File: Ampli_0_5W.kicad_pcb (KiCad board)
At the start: 2 copper layers, 100 x 100 mm, 71 parts, among them J1 RF_In, J2 PTT_In, J3 Aux_PTT_Out, J4 RF_Out, J5 RF_Out, J6 RF_Out, Q1 2N7002, Q2 FDD6685, Q3 2N5109, Q4 AFT05MP075N, T1 4:1, T2 1:1, T3 1:9, U1 LM78M05_TO252

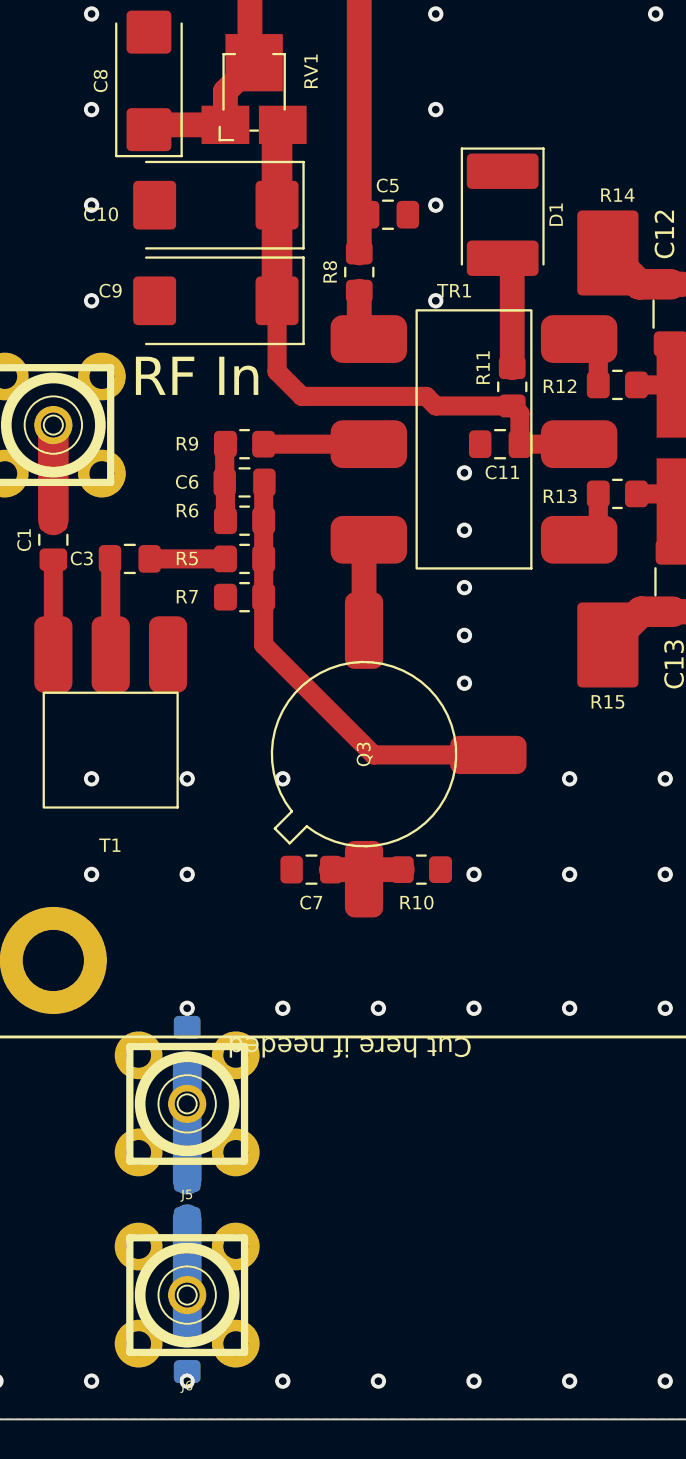
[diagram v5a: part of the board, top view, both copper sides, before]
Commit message: Kicad 7, new iBom, new temp diode cabling
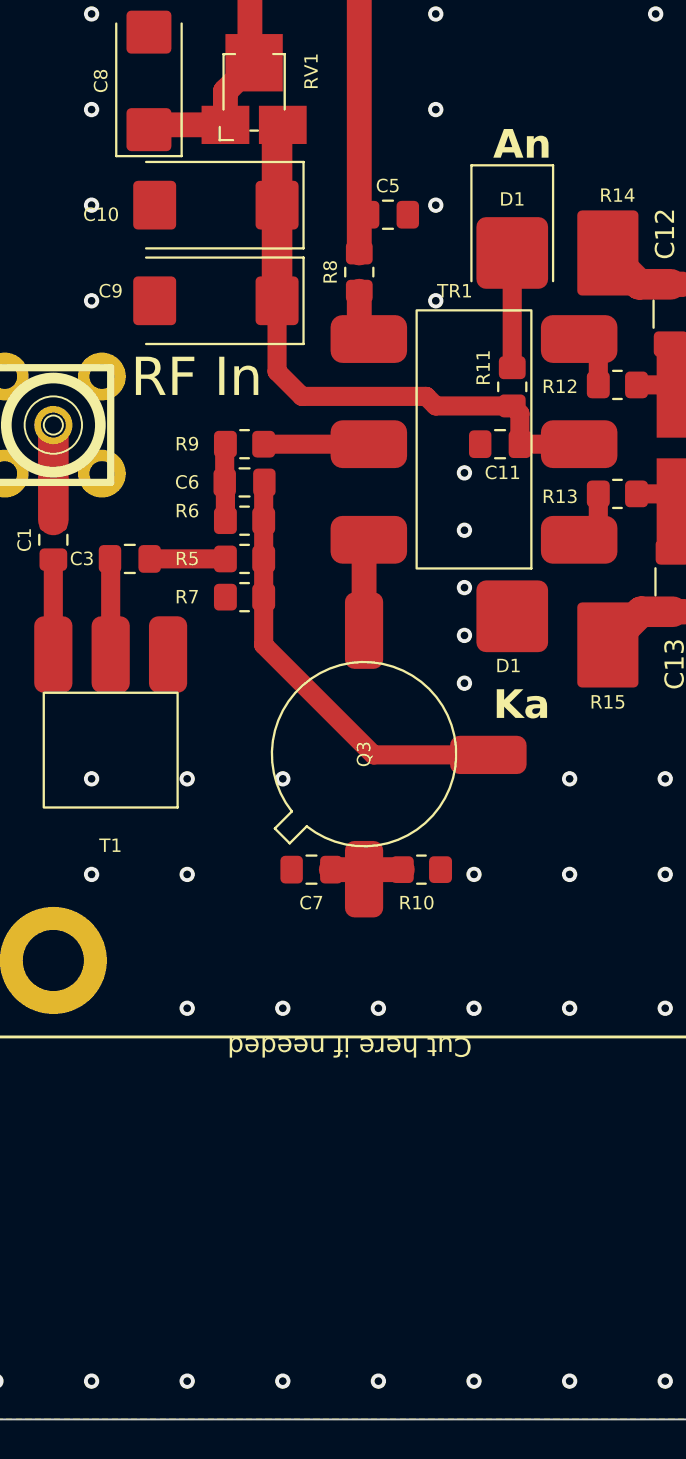
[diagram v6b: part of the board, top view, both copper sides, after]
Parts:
- removed J5, J6: RF_Out, SMA_PINS:SMA_PINS
- removed R16, R18: 62R, Resistor_SMD:R_0805_2012Metric_Pad1.20x1.40mm_HandSolder
- removed R17: 249R, Resistor_SMD:R_0805_2012Metric_Pad1.20x1.40mm_HandSolder
- moved D1 1.01 mm to (109.0, 67.9)
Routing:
- net Net-(J6-Pad1): track 6.00 -> 0.00 mm
- net Net-(J5-Pad1): track 6.00 -> 0.00 mm
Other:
- board text added: "An"
- board text added: "D1"
- board text added: "Ka"
